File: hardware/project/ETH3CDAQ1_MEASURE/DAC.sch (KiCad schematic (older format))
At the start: 19 parts, among them U901 TL074

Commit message: Measurement module development.
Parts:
- added C801, C802: 10u, Capacitor_SMD:C_0805_2012Metric_Pad1.18x1.45mm_HandSolder, symbol Device:C
- added C803, C804, C807: 100n, Capacitor_SMD:C_0603_1608Metric_Pad1.08x0.95mm_HandSolder, symbol Device:C
- added C805, C806: 4u7, Capacitor_SMD:C_0805_2012Metric_Pad1.18x1.45mm_HandSolder, symbol Device:C
- added FB801, FB802: MPZ1608S221ATA00, Resistor_SMD:R_0603_1608Metric_Pad0.98x0.95mm_HandSolder, symbol Device:Ferrite_Bead
- added R801, R802, R803, R804: 27, Resistor_SMD:R_0603_1608Metric_Pad0.98x0.95mm_HandSolder, symbol Device:R
- added R805: 10, Resistor_SMD:R_0603_1608Metric_Pad0.98x0.95mm_HandSolder, symbol Device:R
- added U802: DAC8564, Package_SO:TSSOP-16_4.4x5mm_P0.65mm, symbol ETH3CDAQ1:DAC8564
- added U803: TL071, Package_SO:SOIC-8_3.9x4.9mm_P1.27mm, symbol Amplifier_Operational:TL071
- C808: renamed from C901; footprint (none) -> Capacitor_SMD:C_0603_1608Metric_Pad1.08x0.95mm_HandSolder
- C809: renamed from C902; footprint (none) -> Capacitor_SMD:C_0603_1608Metric_Pad1.08x0.95mm_HandSolder
- C810: renamed from C903; footprint (none) -> Capacitor_SMD:C_0603_1608Metric_Pad1.08x0.95mm_HandSolder
- C811: renamed from C904; footprint (none) -> Capacitor_SMD:C_0603_1608Metric_Pad1.08x0.95mm_HandSolder
- C812: renamed from C905; footprint (none) -> Capacitor_SMD:C_0603_1608Metric_Pad1.08x0.95mm_HandSolder
- C813: renamed from C906; footprint (none) -> Capacitor_SMD:C_0603_1608Metric_Pad1.08x0.95mm_HandSolder
- R806: renamed from R901; footprint (none) -> Resistor_SMD:R_0603_1608Metric_Pad0.98x0.95mm_HandSolder
- R807: renamed from R902; footprint (none) -> Resistor_SMD:R_0603_1608Metric_Pad0.98x0.95mm_HandSolder
- R808: renamed from R903; footprint (none) -> Resistor_SMD:R_0603_1608Metric_Pad0.98x0.95mm_HandSolder
- R809: renamed from R904; footprint (none) -> Resistor_SMD:R_0603_1608Metric_Pad0.98x0.95mm_HandSolder
- R810: renamed from R905; footprint (none) -> Resistor_SMD:R_0603_1608Metric_Pad0.98x0.95mm_HandSolder
- R811: renamed from R906; footprint (none) -> Resistor_SMD:R_0603_1608Metric_Pad0.98x0.95mm_HandSolder
- R812: renamed from R907; footprint (none) -> Resistor_SMD:R_0603_1608Metric_Pad0.98x0.95mm_HandSolder
- R813: renamed from R908; footprint (none) -> Resistor_SMD:R_0603_1608Metric_Pad0.98x0.95mm_HandSolder
- R814: renamed from R909; footprint (none) -> Resistor_SMD:R_0603_1608Metric_Pad0.98x0.95mm_HandSolder
- R815: renamed from R910; footprint (none) -> Resistor_SMD:R_0603_1608Metric_Pad0.98x0.95mm_HandSolder
- R816: renamed from R911; footprint (none) -> Resistor_SMD:R_0603_1608Metric_Pad0.98x0.95mm_HandSolder
- R817: renamed from R912; footprint (none) -> Resistor_SMD:R_0603_1608Metric_Pad0.98x0.95mm_HandSolder
- U801: renamed from U901; footprint (none) -> Package_SO:SOIC-14_3.9x8.7mm_P1.27mm
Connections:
- net +2V5REF: now also C806.1, C807.1, R805.1
- net DAC_0-2V5_VOUT1: now also U802.1 (VOUTA)
- net DAC_0-2V5_VOUT2: now also U802.2 (VOUTB)
- net DAC_0-2V5_VOUT3: now also U802.7 (VOUTC)
- net GNDA: now also C801.2, C802.2, C803.2, C804.2, C805.2, C806.2, C807.2, U802.5 (VREFL), U802.6 (GND), U803.4 (V-)
- net -18V: now reaches U801.11 (V-)
- net +18V: now reaches U801.4 (V+)
- net DAC_VOUT1 renamed DAC_V1
- net DAC_VOUT2 renamed DAC_V2
- net DAC_VOUT3 renamed DAC_V3
- new net: R805.2, U803.2 (-), U803.6
- new net: C805.1, U802.3 (VREFOUT), U803.3 (+)
- new net: R803.1, U802.10 (SCLK)
- new net: R802.1, U802.11 (DIN)
- new net: C801.1, C803.1, FB801.1, U802.12 (IOVDD)
- new net: R804.1, U802.16 (LDAC)
- new net: C802.1, C804.1, FB802.1, U802.4 (AVDD)
- new net: R801.1, U802.9 (~SYNC)
- new net +3V3: FB801.2
- new net +5VF: FB802.2, U803.7 (V+)
- new net DAC_DIN: R802.2
- new net DAC_LDAC: R804.2
- new net DAC_SCLK: R803.2
- new net DAC_~SYNC: R801.2
- new net GND: U802.13 (A0), U802.14 (A1), U802.15 (~ENABLE)
- no-connect marks 0 -> 3

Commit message: PCB layout
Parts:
- removed R801, R802, R803, R804: 27, Resistor_SMD:R_0603_1608Metric_Pad0.98x0.95mm_HandSolder, symbol Device:R
- renumbered R805 to R801, R806 to R802, R807 to R803, R808 to R804, R809 to R805, R810 to R806, R811 to R807, R812 to R808, R813 to R809, R814 to R810, R815 to R811, R816 to R812, R817 to R813
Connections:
- net DAC_DIN: now also U802.11 (DIN)
- net DAC_LDAC: now also U802.16 (LDAC)
- net DAC_SCLK: now also U802.10 (SCLK)
- net DAC_~SYNC: now also U802.9 (~SYNC)
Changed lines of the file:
@@
 $EndComp
 $Comp
-L Device:R R806
+L Device:R R802
 U 1 1 5FB74FFB
 P 8100 900
-F 0 "R806" V 7893 900 50  0000 C CNN
+F 0 "R802" V 7893 900 50  0000 C CNN
 F 1 "1k" V 7984 900 50  0000 C CNN
 F 2 "Resistor_SMD:R_0603_1608Metric_Pad0.98x0.95mm_HandSolder" V 8030 900 50  0001 C CNN
@@
 $EndComp
 $Comp
-L Device:R R809
+L Device:R R805
 U 1 1 5FB764C8
 P 8600 1700
-F 0 "R809" V 8393 1700 50  0000 C CNN
+F 0 "R805" V 8393 1700 50  0000 C CNN
 F 1 "24k9" V 8484 1700 50  0000 C CNN
 F 2 "Resistor_SMD:R_0603_1608Metric_Pad0.98x0.95mm_HandSolder" V 8530 1700 50  0001 C CNN
@@
 $EndComp
 $Comp
-L Device:R R815
+L Device:R R811
 U 1 1 5FB76CE1
 P 9000 1700
-F 0 "R815" V 8793 1700 50  0000 C CNN
+F 0 "R811" V 8793 1700 50  0000 C CNN
 F 1 "100k" V 8884 1700 50  0000 C CNN
 F 2 "Resistor_SMD:R_0603_1608Metric_Pad0.98x0.95mm_HandSolder" V 8930 1700 50  0001 C CNN
@@
 $EndComp
 $Comp
-L Device:R R810
+L Device:R R806
 U 1 1 5FB7736F
 P 8600 2050
-F 0 "R810" V 8393 2050 50  0000 C CNN
+F 0 "R806" V 8393 2050 50  0000 C CNN
 F 1 "33k2" V 8484 2050 50  0000 C CNN
 F 2 "Resistor_SMD:R_0603_1608Metric_Pad0.98x0.95mm_HandSolder" V 8530 2050 50  0001 C CNN
@@
 	7200 900  7950 900
 $Comp
-L Device:R R807
+L Device:R R803
 U 1 1 5FB8ABA6
 P 8100 2550
-F 0 "R807" V 7893 2550 50  0000 C CNN
+F 0 "R803" V 7893 2550 50  0000 C CNN
 F 1 "1k" V 7984 2550 50  0000 C CNN
 F 2 "Resistor_SMD:R_0603_1608Metric_Pad0.98x0.95mm_HandSolder" V 8030 2550 50  0001 C CNN
@@
 $EndComp
 $Comp
-L Device:R R811
+L Device:R R807
 U 1 1 5FB8ABB2
 P 8600 3350
-F 0 "R811" V 8393 3350 50  0000 C CNN
+F 0 "R807" V 8393 3350 50  0000 C CNN
 F 1 "24k9" V 8484 3350 50  0000 C CNN
 F 2 "Resistor_SMD:R_0603_1608Metric_Pad0.98x0.95mm_HandSolder" V 8530 3350 50  0001 C CNN
@@
 $EndComp
 $Comp
-L Device:R R816
+L Device:R R812
 U 1 1 5FB8ABB8
 P 9000 3350
-F 0 "R816" V 8793 3350 50  0000 C CNN
+F 0 "R812" V 8793 3350 50  0000 C CNN
 F 1 "100k" V 8884 3350 50  0000 C CNN
 F 2 "Resistor_SMD:R_0603_1608Metric_Pad0.98x0.95mm_HandSolder" V 8930 3350 50  0001 C CNN
@@
 $EndComp
 $Comp
-L Device:R R812
+L Device:R R808
 U 1 1 5FB8ABBE
 P 8600 3700
-F 0 "R812" V 8393 3700 50  0000 C CNN
+F 0 "R808" V 8393 3700 50  0000 C CNN
 F 1 "33k2" V 8484 3700 50  0000 C CNN
 F 2 "Resistor_SMD:R_0603_1608Metric_Pad0.98x0.95mm_HandSolder" V 8530 3700 50  0001 C CNN
@@
 	7200 2550 7950 2550
 $Comp
-L Device:R R808
+L Device:R R804
 U 1 1 5FB8F6F8
 P 8100 4250
-F 0 "R808" V 7893 4250 50  0000 C CNN
+F 0 "R804" V 7893 4250 50  0000 C CNN
 F 1 "1k" V 7984 4250 50  0000 C CNN
 F 2 "Resistor_SMD:R_0603_1608Metric_Pad0.98x0.95mm_HandSolder" V 8030 4250 50  0001 C CNN
@@
 $EndComp
 $Comp
-L Device:R R813
+L Device:R R809
 U 1 1 5FB8F704
 P 8600 5050
-F 0 "R813" V 8393 5050 50  0000 C CNN
+F 0 "R809" V 8393 5050 50  0000 C CNN
 F 1 "24k9" V 8484 5050 50  0000 C CNN
 F 2 "Resistor_SMD:R_0603_1608Metric_Pad0.98x0.95mm_HandSolder" V 8530 5050 50  0001 C CNN
@@
 $EndComp
 $Comp
-L Device:R R817
+L Device:R R813
 U 1 1 5FB8F70A
 P 9000 5050
-F 0 "R817" V 8793 5050 50  0000 C CNN
+F 0 "R813" V 8793 5050 50  0000 C CNN
 F 1 "100k" V 8884 5050 50  0000 C CNN
 F 2 "Resistor_SMD:R_0603_1608Metric_Pad0.98x0.95mm_HandSolder" V 8930 5050 50  0001 C CNN
@@
 $EndComp
 $Comp
-L Device:R R814
+L Device:R R810
 U 1 1 5FB8F710
 P 8600 5400
-F 0 "R814" V 8393 5400 50  0000 C CNN
+F 0 "R810" V 8393 5400 50  0000 C CNN
 F 1 "33k2" V 8484 5400 50  0000 C CNN
 F 2 "Resistor_SMD:R_0603_1608Metric_Pad0.98x0.95mm_HandSolder" V 8530 5400 50  0001 C CNN
@@
 +2V5REF
 $Comp
-L Device:R R805
+L Device:R R801
 U 1 1 5FE68DD9
 P 5800 4250
-F 0 "R805" V 5593 4250 50  0000 C CNN
+F 0 "R801" V 5593 4250 50  0000 C CNN
 F 1 "10" V 5684 4250 50  0000 C CNN
 F 2 "Resistor_SMD:R_0603_1608Metric_Pad0.98x0.95mm_HandSolder" V 5730 4250 50  0001 C CNN
@@
 Wire Wire Line
 	2650 4050 2650 3950
-$Comp
-L Device:R R804
-U 1 1 5FF83625
-P 2500 3650
-F 0 "R804" V 2450 3300 50  0000 C CNN
-F 1 "27" V 2500 3650 50  0000 C CNN
-F 2 "Resistor_SMD:R_0603_1608Metric_Pad0.98x0.95mm_HandSolder" V 2430 3650 50  0001 C CNN
-F 3 "~" H 2500 3650 50  0001 C CNN
-	1    2500 3650
-	0    1    1    0
-$EndComp
-$Comp
-L Device:R R803
-U 1 1 5FF84494
-P 2500 3550
-F 0 "R803" V 2450 3200 50  0000 C CNN
-F 1 "27" V 2500 3550 50  0000 C CNN
-F 2 "Resistor_SMD:R_0603_1608Metric_Pad0.98x0.95mm_HandSolder" V 2430 3550 50  0001 C CNN
-F 3 "~" H 2500 3550 50  0001 C CNN
-	1    2500 3550
-	0    1    1    0
-$EndComp
-$Comp
-L Device:R R802
-U 1 1 5FF846A2
-P 2500 3450
-F 0 "R802" V 2450 3100 50  0000 C CNN
-F 1 "27" V 2500 3450 50  0000 C CNN
-F 2 "Resistor_SMD:R_0603_1608Metric_Pad0.98x0.95mm_HandSolder" V 2430 3450 50  0001 C CNN
-F 3 "~" H 2500 3450 50  0001 C CNN
-	1    2500 3450
-	0    1    1    0
-$EndComp
-$Comp
-L Device:R R801
-U 1 1 5FF848D1
-P 2500 3350
-F 0 "R801" V 2450 3000 50  0000 C CNN
-F 1 "27" V 2500 3350 50  0000 C CNN
-F 2 "Resistor_SMD:R_0603_1608Metric_Pad0.98x0.95mm_HandSolder" V 2430 3350 50  0001 C CNN
-F 3 "~" H 2500 3350 50  0001 C CNN
-	1    2500 3350
-	0    1    1    0
-$EndComp
-Wire Wire Line
-	2700 3650 2650 3650
-Wire Wire Line
-	2650 3550 2700 3550
-Wire Wire Line
-	2700 3450 2650 3450
-Wire Wire Line
-	2650 3350 2700 3350
-Wire Wire Line
-	2350 3350 2000 3350
-Text HLabel 2000 3350 0    50   Input ~ 0
+Wire Wire Line
+	2700 3350 2350 3350
+Text HLabel 2350 3350 0    50   Input ~ 0
 DAC_~SYNC
-Text HLabel 2000 3450 0    50   Input ~ 0
+Text HLabel 2350 3450 0    50   Input ~ 0
 DAC_DIN
-Text HLabel 2000 3550 0    50   Input ~ 0
+Text HLabel 2350 3550 0    50   Input ~ 0
 DAC_SCLK
-Text HLabel 2000 3650 0    50   Input ~ 0
+Text HLabel 2350 3650 0    50   Input ~ 0
 DAC_LDAC
 Wire Wire Line
-	2000 3650 2350 3650
-Wire Wire Line
-	2350 3550 2000 3550
-Wire Wire Line
-	2000 3450 2350 3450
+	2350 3650 2700 3650
+Wire Wire Line
+	2700 3550 2350 3550
+Wire Wire Line
+	2350 3450 2700 3450
 $Comp
 L ETH3CDAQ1:+18V #PWR0801

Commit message: PCB design
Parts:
- added C814, C815: 100n, Capacitor_SMD:C_0603_1608Metric_Pad1.08x0.95mm_HandSolder, symbol Device:C
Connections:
- net +18V: now also C814.1
- net -18V: now also C815.1
- net GNDA: now also C814.2, C815.2
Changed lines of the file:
@@
 	-1   0    0    1
 $EndComp
+$Comp
+L Device:C C814
+U 1 1 5FBF861E
+P 1600 7000
+F 0 "C814" H 1715 7046 50  0000 L CNN
+F 1 "100n" H 1715 6955 50  0000 L CNN
+F 2 "Capacitor_SMD:C_0603_1608Metric_Pad1.08x0.95mm_HandSolder" H 1638 6850 50  0001 C CNN
+F 3 "~" H 1600 7000 50  0001 C CNN
+	1    1600 7000
+	1    0    0    -1
+$EndComp
+$Comp
+L power:GNDA #PWR0824
+U 1 1 5FBF9BFD
+P 1600 7200
+F 0 "#PWR0824" H 1600 6950 50  0001 C CNN
+F 1 "GNDA" H 1605 7027 50  0000 C CNN
+F 2 "" H 1600 7200 50  0001 C CNN
+F 3 "" H 1600 7200 50  0001 C CNN
+	1    1600 7200
+	1    0    0    -1
+$EndComp
+$Comp
+L ETH3CDAQ1:+18V #PWR0823
+U 1 1 5FBFA3E4
+P 1600 6800
+F 0 "#PWR0823" H 1600 6650 50  0001 C CNN
+F 1 "+18V" H 1615 6973 50  0000 C CNN
+F 2 "" H 1600 6800 50  0001 C CNN
+F 3 "" H 1600 6800 50  0001 C CNN
+	1    1600 6800
+	1    0    0    -1
+$EndComp
+Wire Wire Line
+	1600 6800 1600 6850
+Wire Wire Line
+	1600 7150 1600 7200
+$Comp
+L Device:C C815
+U 1 1 5FC00BE3
+P 2100 7000
+F 0 "C815" H 2215 7046 50  0000 L CNN
+F 1 "100n" H 2215 6955 50  0000 L CNN
+F 2 "Capacitor_SMD:C_0603_1608Metric_Pad1.08x0.95mm_HandSolder" H 2138 6850 50  0001 C CNN
+F 3 "~" H 2100 7000 50  0001 C CNN
+	1    2100 7000
+	1    0    0    -1
+$EndComp
+$Comp
+L power:GNDA #PWR0826
+U 1 1 5FC00BE9
+P 2100 7200
+F 0 "#PWR0826" H 2100 6950 50  0001 C CNN
+F 1 "GNDA" H 2105 7027 50  0000 C CNN
+F 2 "" H 2100 7200 50  0001 C CNN
+F 3 "" H 2100 7200 50  0001 C CNN
+	1    2100 7200
+	1    0    0    -1
+$EndComp
+Wire Wire Line
+	2100 7150 2100 7200
+$Comp
+L ETH3CDAQ1:-18V #PWR0825
+U 1 1 5FC060A3
+P 2100 6800
+F 0 "#PWR0825" H 2100 6650 50  0001 C CNN
+F 1 "-18V" H 2115 6973 50  0000 C CNN
+F 2 "" H 2100 6800 50  0001 C CNN
+F 3 "" H 2100 6800 50  0001 C CNN
+	1    2100 6800
+	1    0    0    -1
+$EndComp
+Wire Wire Line
+	2100 6800 2100 6850
 $EndSCHEMATC

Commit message: PCB layout
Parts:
- renumbered C814 to C1301, C815 to C1302, C801 to C1303, C802 to C1304, C803 to C1305, C804 to C1306, C805 to C1307, C806 to C1308, C807 to C1309, C808 to C1310, C809 to C1311, C810 to C1312, C811 to C1313, C812 to C1314, C813 to C1315, FB801 to FB1301, FB802 to FB1302, R801 to R1301, R802 to R1302, R803 to R1303, R804 to R1304, R805 to R1305, R806 to R1306, R807 to R1307, R808 to R1308, R809 to R1309, R810 to R1310, R811 to R1311, R812 to R1312, R813 to R1313, U801 to U1301, U802 to U1302, U803 to U1303

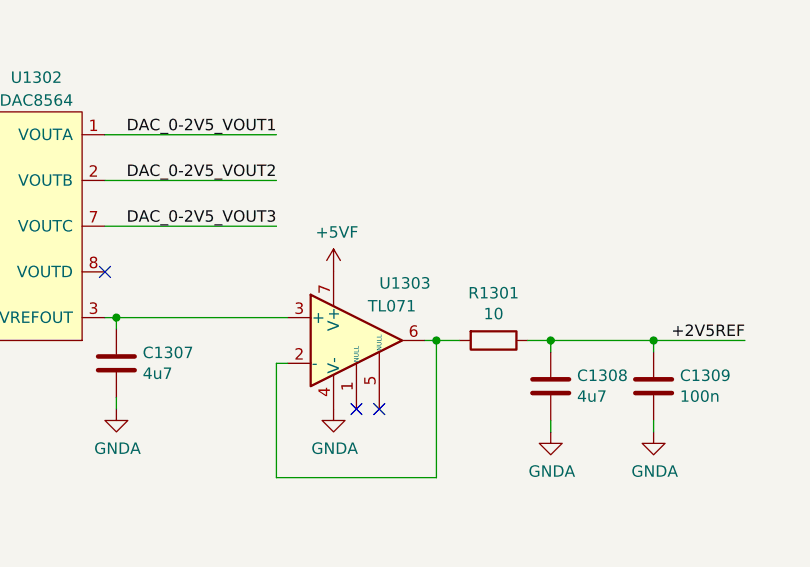
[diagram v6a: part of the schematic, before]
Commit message: Modification in PCBs. Created BOM files.
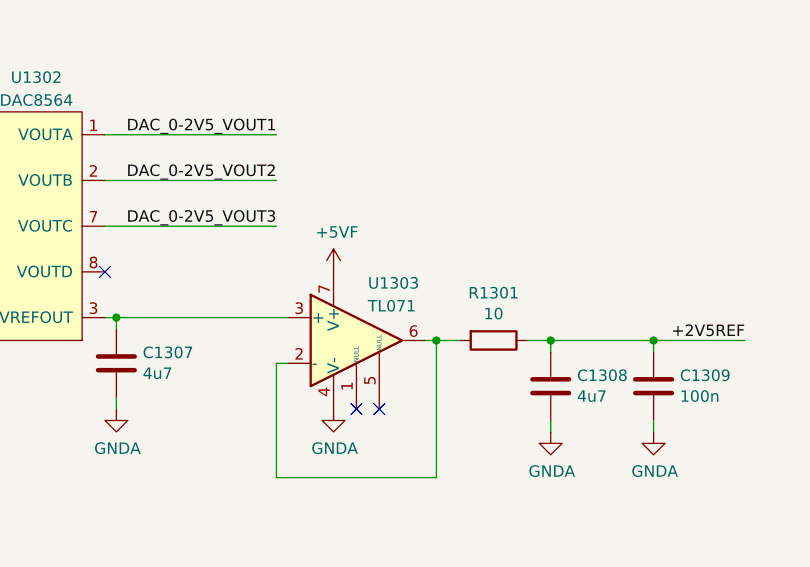
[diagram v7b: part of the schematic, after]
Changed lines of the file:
@@
 U 1 1 5FE58451
 P 5200 4250
-F 0 "U1303" H 5300 4500 50  0000 L CNN
+F 0 "U1303" H 5250 4500 50  0000 L CNN
 F 1 "TL071" H 5250 4400 50  0000 L CNN
 F 2 "Package_SO:SOIC-8_3.9x4.9mm_P1.27mm" H 5250 4300 50  0001 C CNN
